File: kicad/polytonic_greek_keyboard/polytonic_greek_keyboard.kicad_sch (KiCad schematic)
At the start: 0 parts

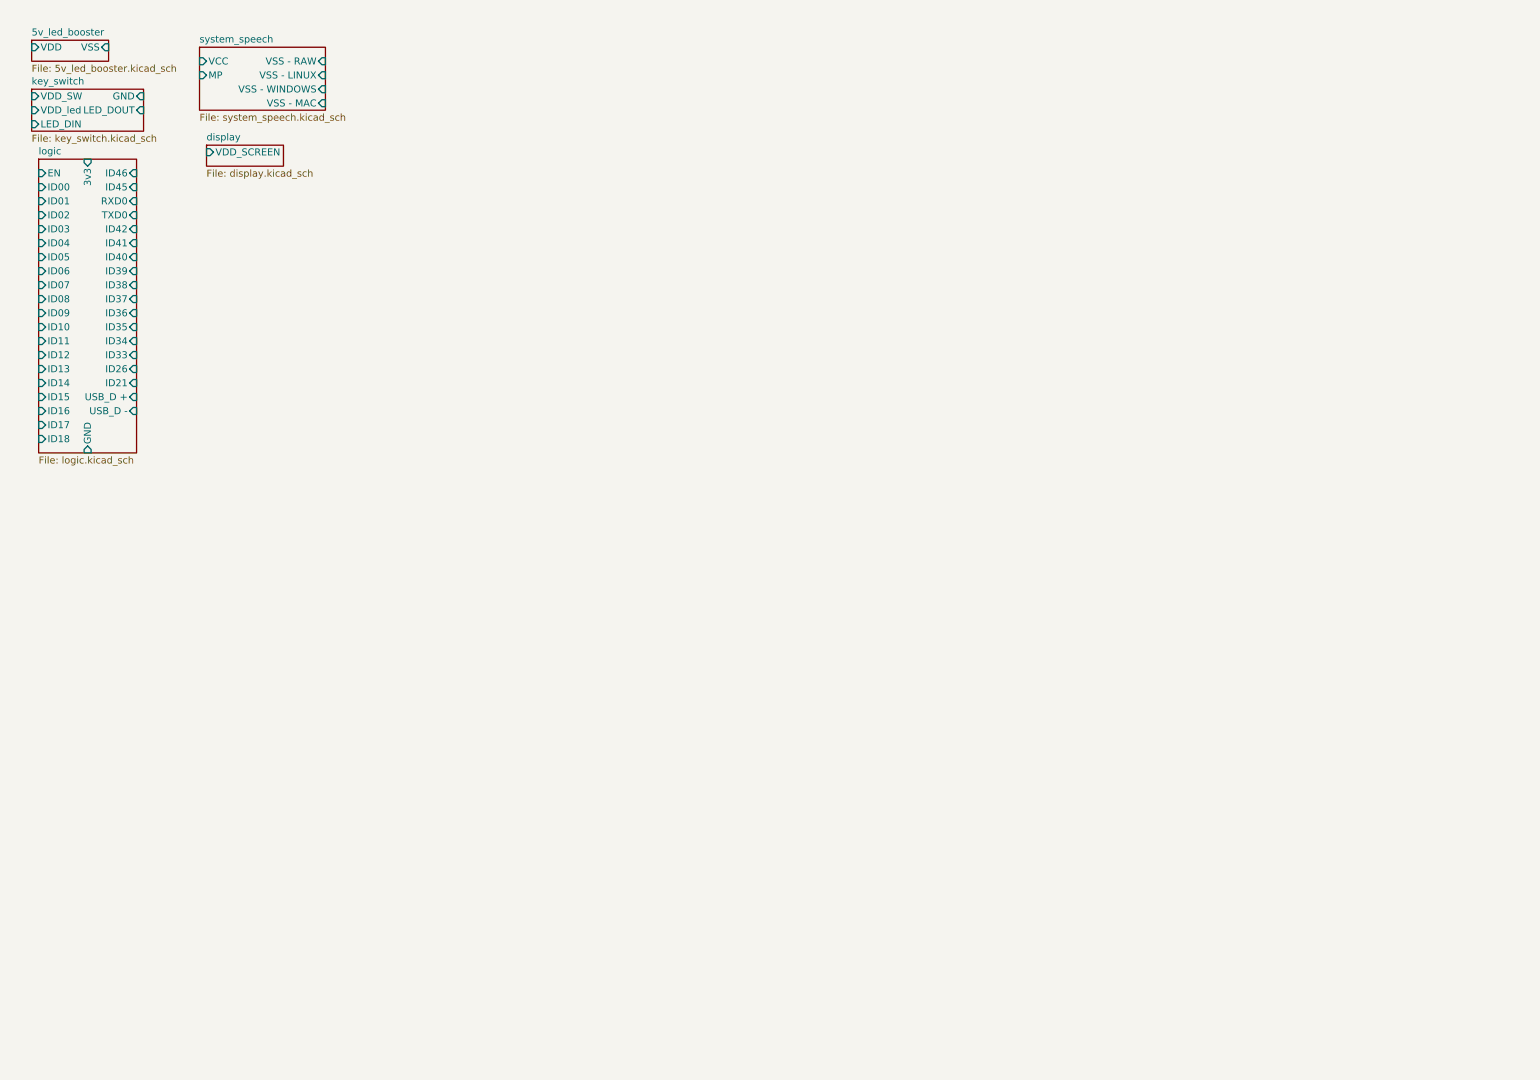
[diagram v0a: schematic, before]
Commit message: [ADD] an initial matrix of what the keyboard will look like logically
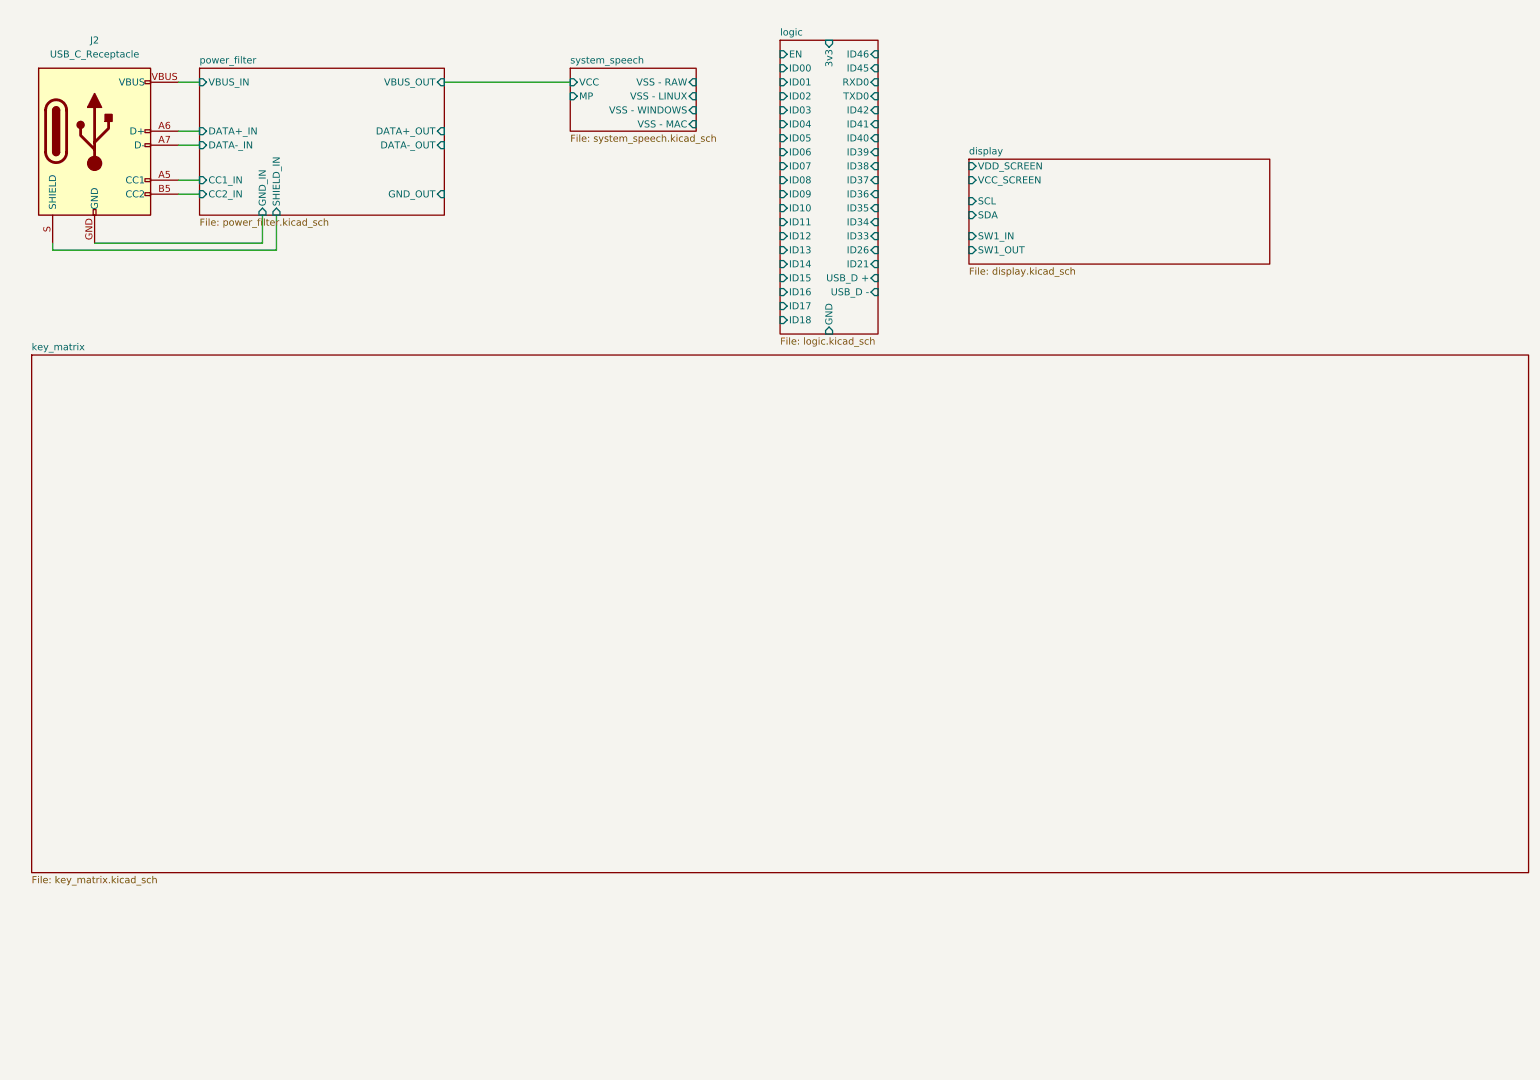
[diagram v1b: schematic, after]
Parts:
- added J2: USB_C_Receptacle, PCM_SparkFun-Connector:USB-C_16, symbol PCM_SparkFun-Connector:USB_C_Receptacle
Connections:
- new net power_filter/CC1_IN: J2.A5 (CC1)
- new net power_filter/CC2_IN: J2.B5 (CC2)
- new net power_filter/DATA+_IN: J2.A6 (D+), J2.B6 (D+)
- new net power_filter/DATA-_IN: J2.A7 (D-), J2.B7 (D-)
- new net power_filter/GND_IN: J2.GND
- new net power_filter/SHIELD_IN: J2.S (SHIELD)
- new net power_filter/VBUS_IN: J2.VBUS
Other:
- removed sheet 5v_led_booster
- removed sheet key_switch
- added sheet key_matrix (key_matrix.kicad_sch)
- added sheet power_filter (power_filter.kicad_sch)
- sheet display ports: added SCL, SDA, SW1_IN, SW1_OUT, VCC_SCREEN; removed none

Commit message: [ADD] a more structured approach of the pcb in a way that won't overload the esp32 that is running it
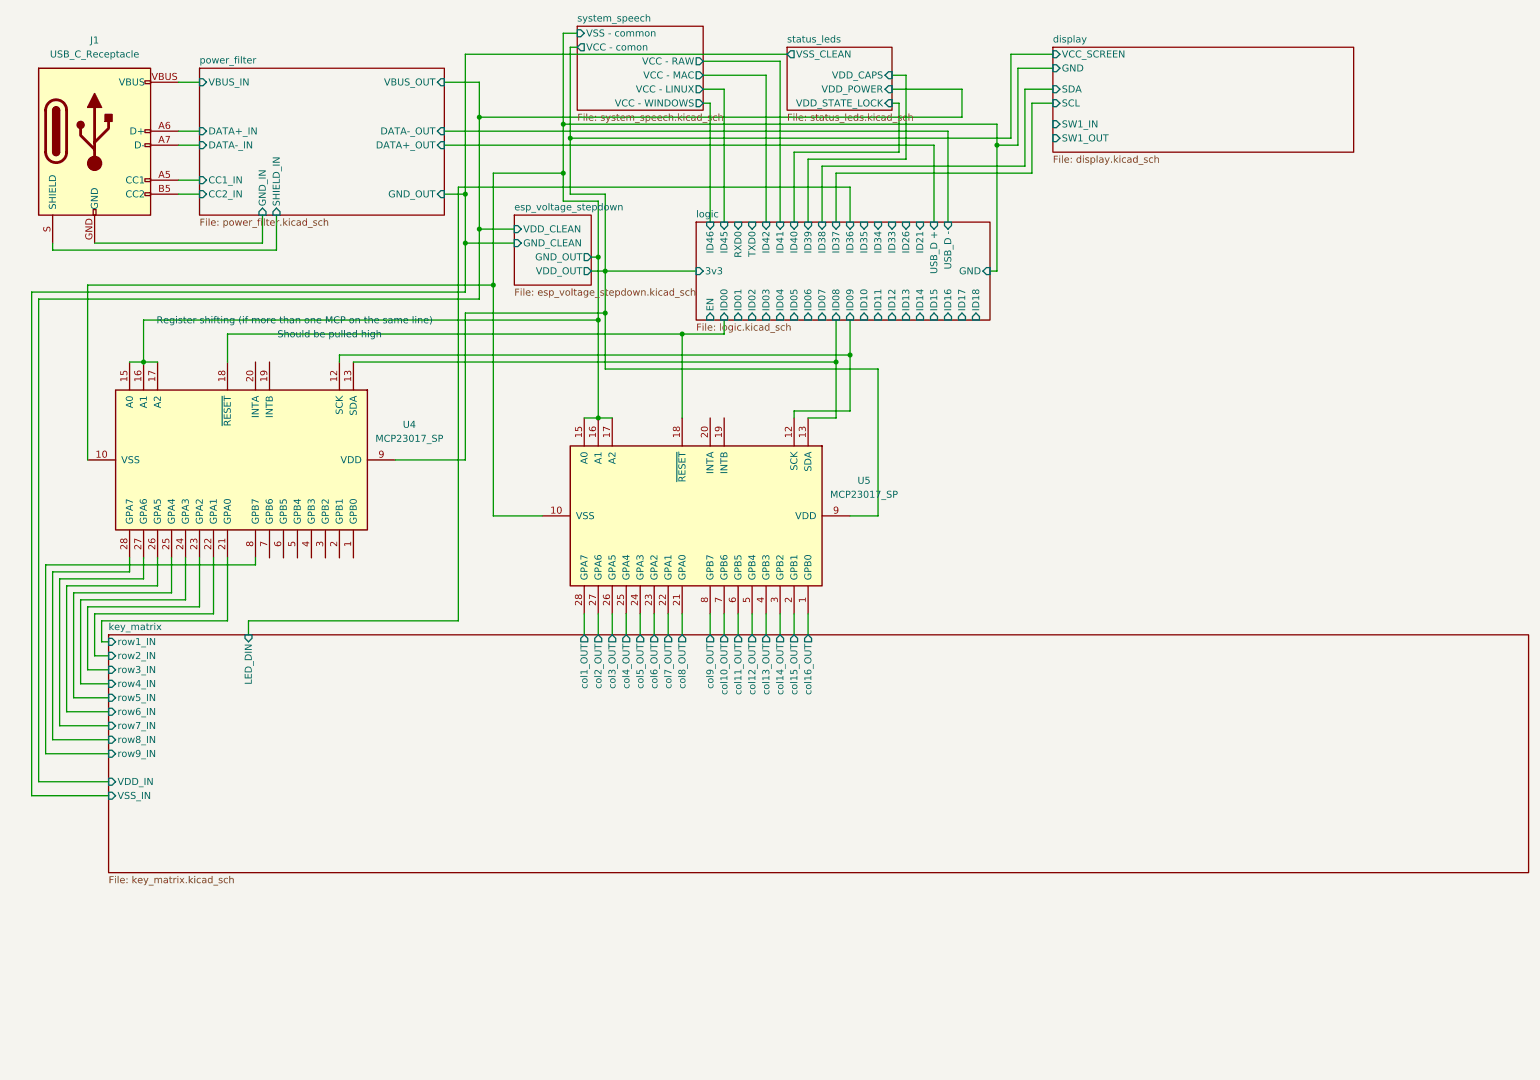
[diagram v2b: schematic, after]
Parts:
- added U4, U5: MCP23017_SP, Package_DIP:DIP-28_W7.62mm, symbol Interface_Expansion:MCP23017_SP
- renumbered J2 to J1
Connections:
- net display/VCC_SCREEN: now also U4.9 (VDD), U5.9 (VDD)
- net logic/ID00: now also U4.18 (~{RESET}), U5.18 (~{RESET})
- net logic/ID08: now also U4.13 (SDA), U5.13 (SDA)
- net logic/ID09: now also U4.12 (SCK), U5.12 (SCK)
- new net display/GND: U4.10 (VSS), U4.15 (A0), U4.16 (A1), U4.17 (A2), U5.10 (VSS), U5.15 (A0), U5.16 (A1), U5.17 (A2)
- new net key_matrix/col10_OUT: U5.7 (GPB6)
- new net key_matrix/col11_OUT: U5.6 (GPB5)
- new net key_matrix/col12_OUT: U5.5 (GPB4)
- new net key_matrix/col13_OUT: U5.4 (GPB3)
- new net key_matrix/col14_OUT: U5.3 (GPB2)
- new net key_matrix/col15_OUT: U5.2 (GPB1)
- new net key_matrix/col16_OUT: U5.1 (GPB0)
- new net key_matrix/col1_OUT: U5.28 (GPA7)
- new net key_matrix/col2_OUT: U5.27 (GPA6)
- new net key_matrix/col3_OUT: U5.26 (GPA5)
- new net key_matrix/col4_OUT: U5.25 (GPA4)
- new net key_matrix/col5_OUT: U5.24 (GPA3)
- new net key_matrix/col6_OUT: U5.23 (GPA2)
- new net key_matrix/col7_OUT: U5.22 (GPA1)
- new net key_matrix/col8_OUT: U5.21 (GPA0)
- new net key_matrix/col9_OUT: U5.8 (GPB7)
- new net key_matrix/row1_IN: U4.21 (GPA0)
- new net key_matrix/row2_IN: U4.22 (GPA1)
- new net key_matrix/row3_IN: U4.23 (GPA2)
- new net key_matrix/row4_IN: U4.24 (GPA3)
- new net key_matrix/row5_IN: U4.25 (GPA4)
- new net key_matrix/row6_IN: U4.26 (GPA5)
- new net key_matrix/row7_IN: U4.27 (GPA6)
- new net key_matrix/row8_IN: U4.28 (GPA7)
- new net key_matrix/row9_IN: U4.8 (GPB7)
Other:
- added sheet esp_voltage_stepdown (esp_voltage_stepdown.kicad_sch)
- added sheet status_leds (status_leds.kicad_sch)
- sheet display ports: added GND; removed VDD_SCREEN
- sheet key_matrix ports: added LED_DIN, VDD_IN, VSS_IN, col10_OUT, col11_OUT, col12_OUT, col13_OUT, col14_OUT, col15_OUT, col16_OUT, col1_OUT, col2_OUT, col3_OUT, col4_OUT, col5_OUT, col6_OUT, col7_OUT, col8_OUT, col9_OUT, row1_IN, row2_IN, row3_IN, row4_IN, row5_IN, row6_IN, row7_IN, row8_IN, row9_IN; removed none
- sheet system_speech ports: added VCC - LINUX, VCC - MAC, VCC - RAW, VCC - WINDOWS, VCC - comon, VSS - common; removed MP, VCC, VSS - LINUX, VSS - MAC, VSS - RAW, VSS - WINDOWS
- note added: "Register shifting (if more than one MCP on the same line)"
- note added: "Should be pulled high"
- title: (none) -> Main level

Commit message: [UPDATE] the board desing, [FIX] connection issues
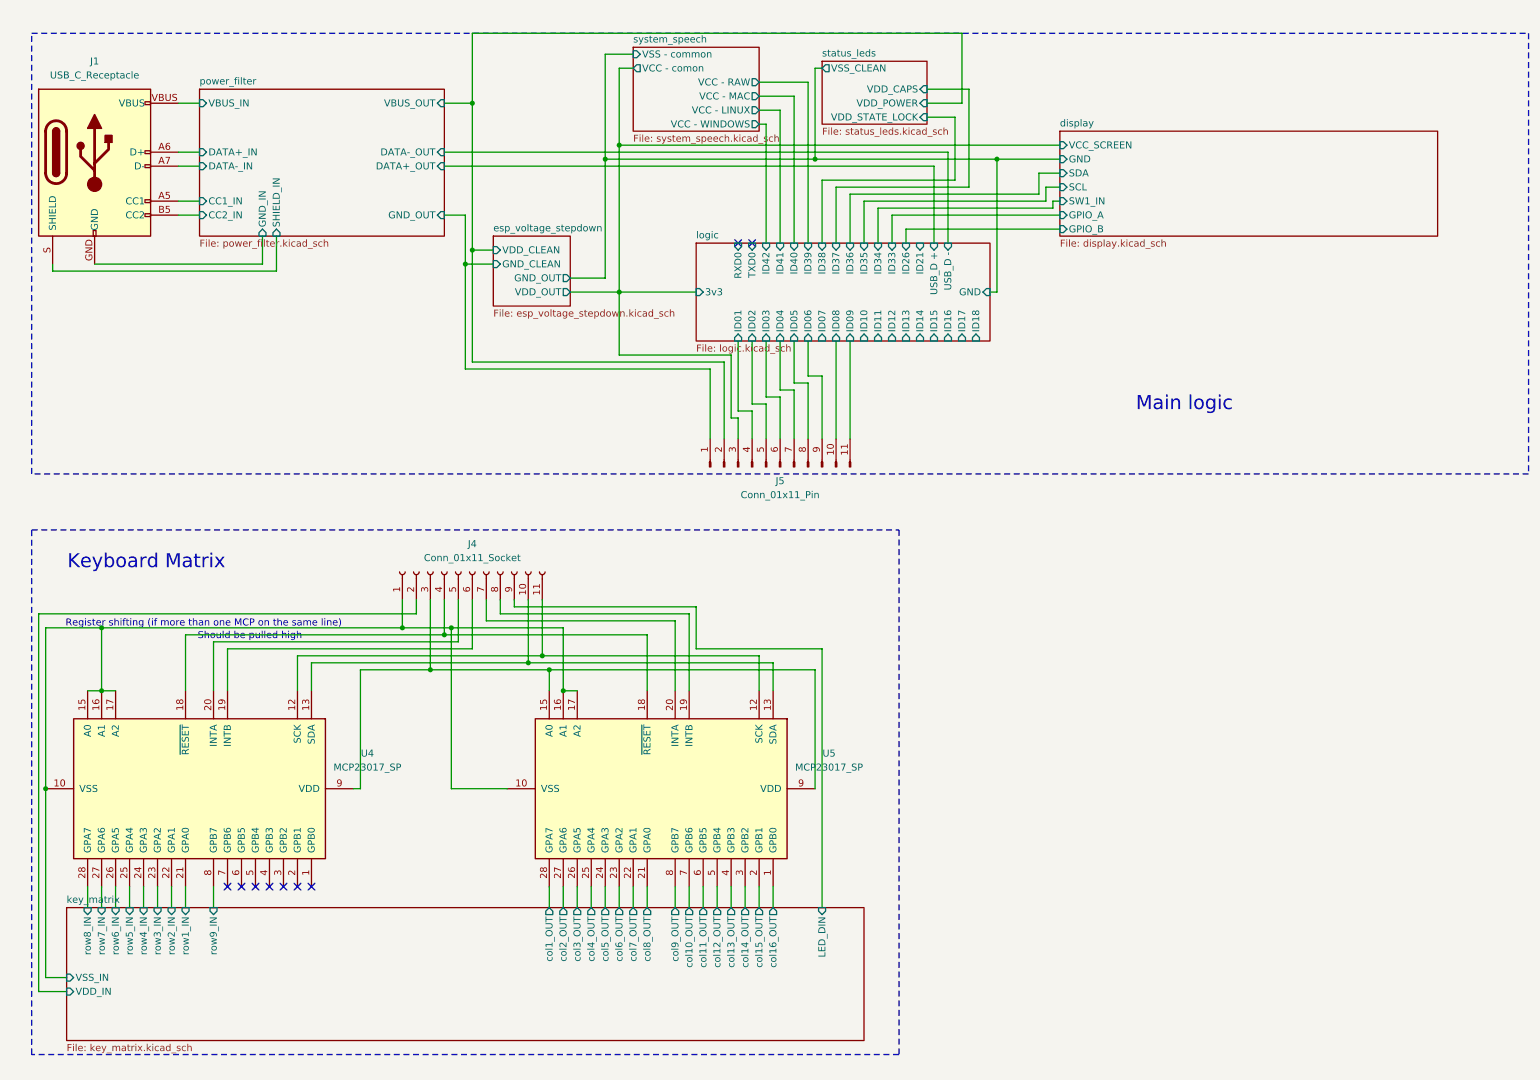
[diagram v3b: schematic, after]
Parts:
- added J4: Conn_01x11_Socket, Connector_PinSocket_2.00mm:PinSocket_1x11_P2.00mm_Horizontal, symbol Connector:Conn_01x11_Socket
- added J5: Conn_01x11_Pin, Connector_PinHeader_2.00mm:PinHeader_1x11_P2.00mm_Horizontal, symbol Connector:Conn_01x11_Pin
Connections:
- net display/GND: no longer U4.10 (VSS), U4.15 (A0), U4.16 (A1), U4.17 (A2), U5.10 (VSS), U5.15 (A0), U5.16 (A1), U5.17 (A2)
- net display/VCC_SCREEN: now also J5.3 (Pin_3); no longer U4.9 (VDD), U5.9 (VDD)
- net esp_voltage_stepdown/GND_CLEAN: now also J5.1 (Pin_1)
- net esp_voltage_stepdown/VDD_CLEAN: now also J5.2 (Pin_2)
- net key_matrix/LED_DIN: now also J4.9 (Pin_9)
- net logic/ID01: now also J5.4 (Pin_4)
- net logic/ID02: now also J5.5 (Pin_5)
- net logic/ID03: now also J5.6 (Pin_6)
- net logic/ID04: now also J5.7 (Pin_7)
- net logic/ID05: now also J5.8 (Pin_8)
- net logic/ID06: now also J5.9 (Pin_9)
- net logic/ID08: now also J5.10 (Pin_10); no longer U4.13 (SDA), U5.13 (SDA)
- net logic/ID09: now also J5.11 (Pin_11); no longer U4.12 (SCK), U5.12 (SCK)
- net at U5.19 (INTB): now also J4.8 (Pin_8)
- net at U5.20 (INTA): now also J4.7 (Pin_7)
- net at U4.19 (INTB): now also J4.6 (Pin_6)
- net at U4.20 (INTA): now also J4.5 (Pin_5)
- net logic/ID00: no longer names the net of U4.18 (~{RESET}), U5.18 (~{RESET})
- net logic/ID00: now also J4.4 (Pin_4)
- new net: J4.11 (Pin_11), U4.12 (SCK), U5.12 (SCK)
- new net: J4.10 (Pin_10), U4.13 (SDA), U5.13 (SDA)
- new net: J4.3 (Pin_3), U4.9 (VDD), U5.15 (A0), U5.9 (VDD)
- new net key_matrix/VDD_IN: J4.2 (Pin_2)
- new net key_matrix/VSS_IN: J4.1 (Pin_1), U4.10 (VSS), U4.15 (A0), U4.16 (A1), U4.17 (A2), U5.10 (VSS), U5.16 (A1), U5.17 (A2)
- no-connect marks 0 -> 9
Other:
- sheet display ports: added GPIO_A, GPIO_B; removed SW1_OUT
- sheet logic ports: added none; removed EN, ID00, ID45, ID46
- note added: "Keyboard Matrix"
- note added: "Main logic"
- moved on the sheet: J1, U4, U5
